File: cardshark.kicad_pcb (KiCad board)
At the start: 4 copper layers, 237 x 69.5 mm, 94 parts, among them J1 Conn_02x03_Odd_Even, J2 Bus_ISA_8bit, J3 DE15_Receptacle_HighDensity_M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, U1 LM334M, U10 SN74F260DR, U11 93CxxA, U12 SOJ_256Kx16, U13 SOJ_256Kx16, U14 27C010, U2 GD543x_VLB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

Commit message: Add files via upload
A bunch of quick changes
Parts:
- moved R8 9.28 mm to (114.9, 105.8), turned to 90 degrees
- moved U11 2.54 mm to (121.5, 105.0)
- moved C33 1.57 mm to (126.2, 105.5)
- moved C17 0.93 mm to (109.3, 116.3)
- moved R29 0.88 mm to (82.5, 73.2)
- moved C22 0.68 mm to (104.7, 116.1)
- moved R6 0.42 mm to (101.0, 104.2)
- moved C2 0.32 mm to (71.8, 94.4)
- moved C16 0.15 mm to (104.8, 101.9)
- moved R1 0.10 mm to (105.5, 106.4)
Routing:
- net GND: track 235.5 -> 242.7 mm, vias 453 -> 538
- net /EECS: track 15.7 -> 22.0 mm, vias 0 -> 2
- net /VCC: track 291.2 -> 295.0 mm
- net /CAS2: track 76.1 -> 79.2 mm
- net /EVIDEO: track 28.0 -> 25.0 mm, vias 2 -> 0
- net /DAT5: track 27.7 -> 30.6 mm
- net /DAT1: track 35.2 -> 37.8 mm
- net /DAT3: track 32.0 -> 34.1 mm
- net Net-(J3-Pad12): track 183.5 -> 185.5 mm
- net /VSYNC: track 175.7 -> 173.9 mm
- net /CAS1: track 130.1 -> 131.9 mm
- net /MD8: track 110.5 -> 112.4 mm
- net /MD9: track 109.4 -> 111.2 mm
- net /MD10: track 111.1 -> 112.9 mm
- net /MD12: track 113.3 -> 115.1 mm
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
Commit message: Add files via upload
Cleaned up PCB graphics to make them actually vaguely fabbable
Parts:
- moved G*** 0.68 mm to (200.5, 101.8)

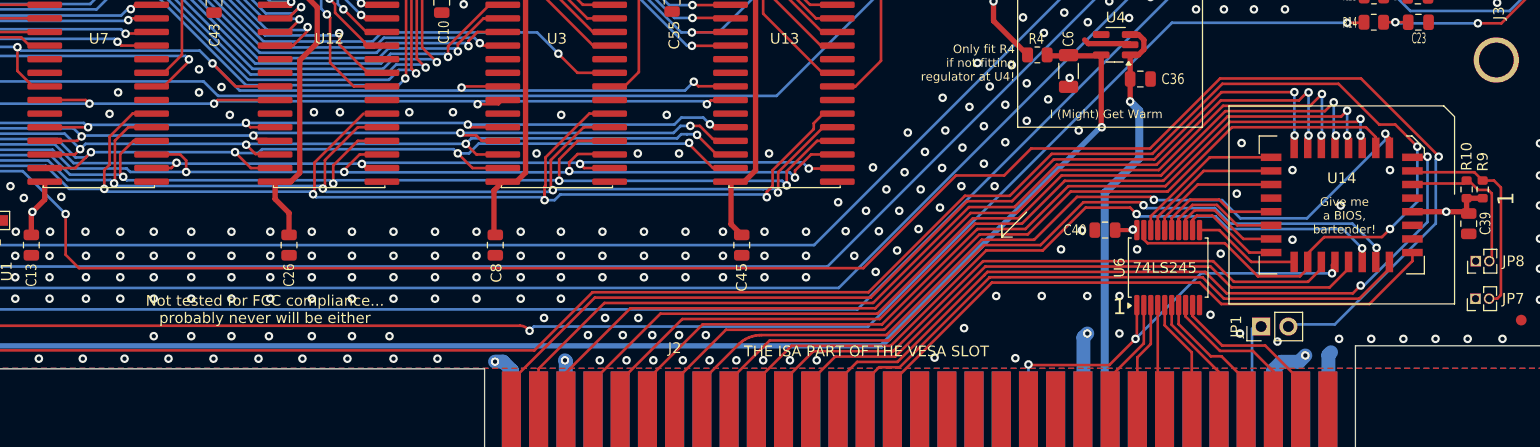
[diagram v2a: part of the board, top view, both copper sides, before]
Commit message: Add files via upload
Hasty bug-fix to a nasty broken PLCC-32 socket problem
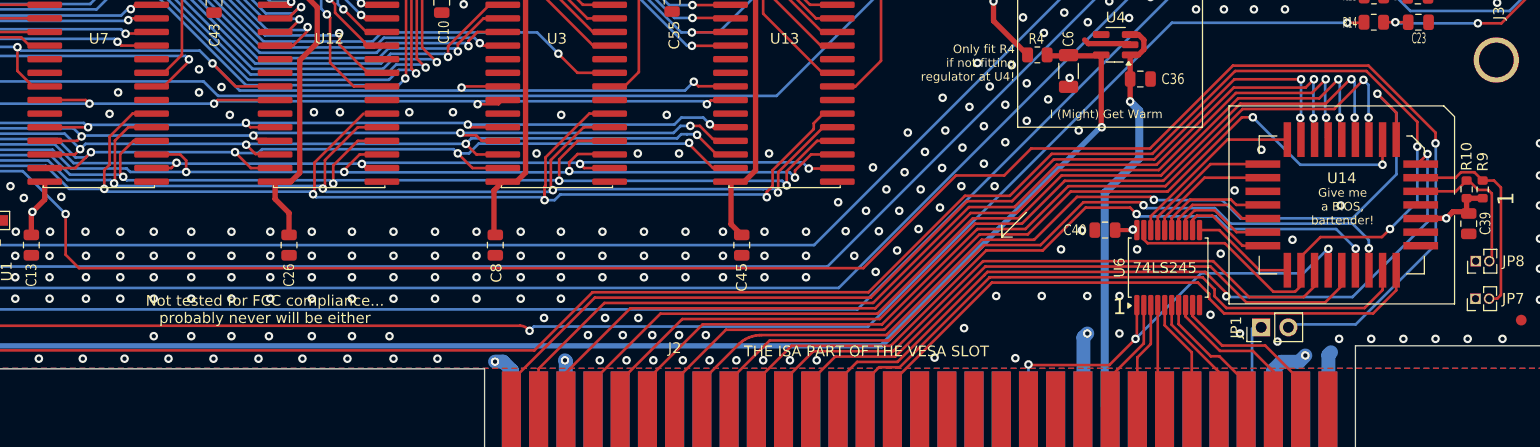
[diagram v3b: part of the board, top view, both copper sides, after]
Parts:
- moved JP1 0.08 mm to (247.5, 127.7)
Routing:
- net /SA7: track 76.7 -> 87.6 mm
- net /EROM: track 245.1 -> 250.8 mm
- net /SA5: track 79.2 -> 84.2 mm
- net /SA4: track 81.6 -> 85.7 mm
- net /SA6: track 76.6 -> 80.4 mm, vias 0 -> 2
- net /IRQ: track 233.9 -> 237.0 mm
- net /SA3: track 84.2 -> 87.0 mm
- net /BD0: track 14.8 -> 17.0 mm
- net /SA2: track 86.4 -> 88.0 mm
- net /SA0: track 89.4 -> 91.1 mm
- net /SA1: track 91.7 -> 93.3 mm
- net /SA13: track 54.9 -> 56.4 mm
- net /~{SMEMRD}: track 40.7 -> 42.2 mm
- net /SA10: track 56.1 -> 57.5 mm
- net /SA11: track 56.2 -> 57.5 mm
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
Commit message: Add files via upload
Big bunch'o little minor fixes, no version number change (mostly to clean up libraries and eliminate a bunch of previously silenced ERC warnings)
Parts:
- removed U1: LM334M, Package_SO:SOIC-8_3.9x4.9mm_P1.27mm
- removed U14: 27C010, PLCC-32:PLCC-32_SMD-Socket
- added U5: 27C010, PDVGA:PLCC-32_SMD-Socket, F.Cu at (255.0, 116.3)
- added U9: LM334M, PDVGA:SOIC-8_DMP-8, F.Cu at (127.0, 121.0)
- R10, R29, R30, R7, R8, R9: footprint Resistor_SMD:R_0603_1608Metric -> Resistor_SMD:R_0805_2012Metric
- RN2: footprint Resistor_SMD:R_Array_Convex_4x0603 -> PDVGA:ResArray_Convex_4x0603
- U11: footprint Package_SO:SOIC-8_3.9x4.9mm_P1.27mm -> PDVGA:SOIC-8_DMP-8
- U12, U13, U3, U7: footprint SOJ_DRAM:SOJ-40_10.16x26.44mm_P1.27mm -> PDVGA:SOJ-40_10.16x26.44mm_P1.27mm
- moved D1 2.60 mm to (128.8, 115.1)
- moved R32 2.54 mm to (127.8, 113.2)
- moved R31 2.50 mm to (127.8, 111.3)
- moved C33 1.15 mm to (127.4, 105.6)
- moved RN2 0.97 mm to (206.6, 81.3)
- moved R9 0.85 mm to (269.0, 114.8)
- moved R7 0.55 mm to (109.5, 100.4)
- moved R8 0.38 mm to (114.5, 105.8)
- moved R10 0.25 mm to (266.9, 114.8)
- moved R30 0.25 mm to (63.0, 75.5)
- moved C39 0.25 mm to (266.9, 118.2)
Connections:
- U8 pad A21: /ADR30 -> unconnected-(U8-A30-PadA21)_1
- U8 pad A22: /ADR28 -> unconnected-(U8-A28-PadA22)_1
- U8 pad B23: /ADR29 -> unconnected-(U8-A29-PadB23)
- U8 pad B24: /ADR27 -> unconnected-(U8-A27-PadB24)
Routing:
- net Net-(D1-A): track 16.8 -> 25.7 mm
- net A16: track 13.4 -> 15.3 mm
- net /VCC: track 294.5 -> 296.4 mm
- net /IREF: track 26.5 -> 25.2 mm
- net A15: track 19.6 -> 20.6 mm
- net /P1: track 8.40 -> 7.72 mm
- net Net-(R31-Pad2): track 6.15 -> 6.81 mm
- net /EVIDEO: track 25.0 -> 25.7 mm
- net /CAS7: track 174.2 -> 174.8 mm
